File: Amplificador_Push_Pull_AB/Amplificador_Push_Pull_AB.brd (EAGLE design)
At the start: 99 x 49.8 mm, 51 parts, among them IC1 LM741P, IC3 788TV, P2 10k, Q1 BC547, Q10 TIP42C, Q2 BC547, Q4 BC547, Q7 BC547, Q8 BC547, T2 2SC1307

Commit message: Error found and corrected.
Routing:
- net P1: track 61.7 -> 60.9 mm
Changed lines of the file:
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@@
 <wire x1="50.8" y1="25.4" x2="53.975" y2="28.575" width="0.8128" layer="16"/>
 <wire x1="49.53" y1="24.13" x2="50.8" y2="25.4" width="0.8128" layer="16"/>
-<wire x1="43.18" y1="18.415" x2="49.53" y2="18.415" width="0.8128" layer="16"/>
 <wire x1="20.32" y1="8.255" x2="17.145" y2="11.43" width="0.8128" layer="16"/>
 <wire x1="17.145" y1="11.43" x2="17.145" y2="12.065" width="0.8128" layer="16"/>
-<wire x1="43.18" y1="18.415" x2="42.545" y2="17.78" width="0.8128" layer="16"/>
-<wire x1="42.545" y1="17.78" x2="42.545" y2="16.51" width="0.8128" layer="16"/>
-<wire x1="42.545" y1="16.51" x2="39.37" y2="13.335" width="0.8128" layer="16"/>
+<wire x1="44.45" y1="18.415" x2="39.37" y2="13.335" width="0.8128" layer="16"/>
 <wire x1="39.37" y1="13.335" x2="39.37" y2="12.065" width="0.8128" layer="16"/>
 <wire x1="39.37" y1="12.065" x2="37.465" y2="10.16" width="0.8128" layer="16"/>
 <wire x1="37.465" y1="10.16" x2="37.465" y2="8.255" width="0.8128" layer="16"/>
+<wire x1="44.45" y1="18.415" x2="49.53" y2="18.415" width="0.8128" layer="16"/>
 </signal>
 <signal name="N$15">
@@
 <wire x1="29.21" y1="11.43" x2="27.94" y2="10.16" width="0.8128" layer="16"/>
 <wire x1="27.94" y1="10.16" x2="27.94" y2="7.62" width="0.8128" layer="16"/>
-<wire x1="21.59" y1="2.54" x2="36.83" y2="2.54" width="1.27" layer="16"/>
-<wire x1="36.83" y1="2.54" x2="37.465" y2="3.175" width="0.8128" layer="16"/>
-<wire x1="37.465" y1="3.175" x2="42.545" y2="3.175" width="0.8128" layer="16"/>
+<wire x1="21.59" y1="2.54" x2="41.91" y2="2.54" width="1.27" layer="16"/>
 <wire x1="54.61" y1="17.78" x2="51.435" y2="14.605" width="1.27" layer="16"/>
 <wire x1="51.435" y1="14.605" x2="49.53" y2="14.605" width="1.27" layer="16"/>
@@
 <wire x1="43.18" y1="8.255" x2="42.545" y2="8.255" width="1.27" layer="16"/>
 <wire x1="57.785" y1="14.605" x2="57.785" y2="17.78" width="0.8128" layer="16"/>
+<wire x1="41.91" y1="2.54" x2="42.545" y2="3.175" width="1.27" layer="16"/>
 </signal>
 <signal name="N$23">

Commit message: Separate fround line done. Its resistance is approximately 0.1 ohm. Schematic connections integrity verified. Check DRC next time!
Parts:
- moved C1 2.54 mm to (81.3, 41.9)
- moved VCC 1.27 mm to (5.71, 33.0)
- moved RCA1 0.64 mm to (17.8, 45.1)
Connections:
- net N$24 renamed +5V
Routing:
- net GND: track 270.7 -> 364.1 mm
- net N$5: track 27.2 -> 30.6 mm
- net VOUT: track 57.4 -> 59.5 mm
- net -18V: track 177.1 -> 175.8 mm
- net +18V: track 162.7 -> 163.4 mm
- net HEHEAH: track 66.6 -> 65.8 mm
- removed copper zone on layer 16, net GND

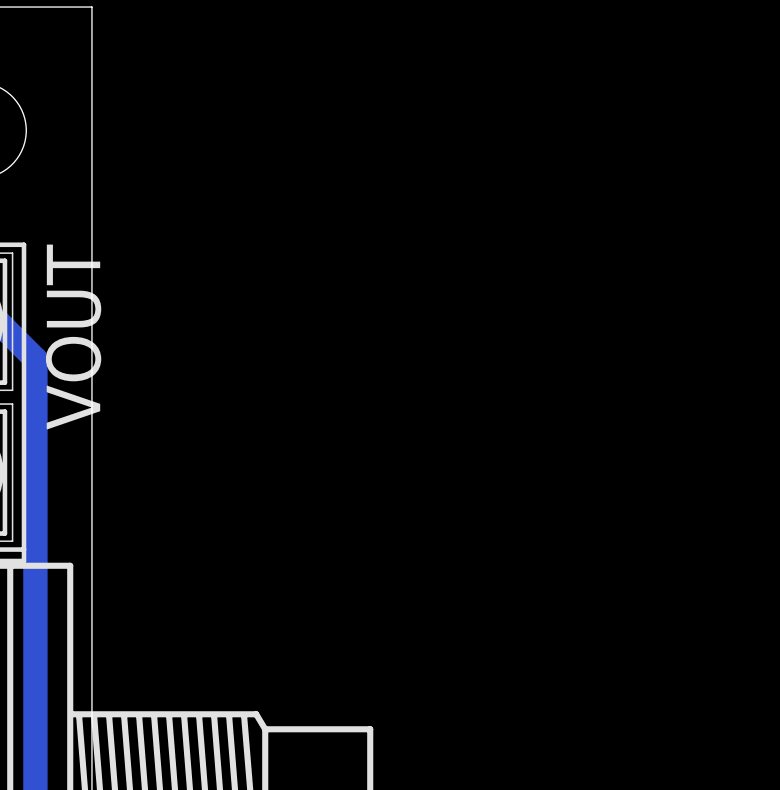
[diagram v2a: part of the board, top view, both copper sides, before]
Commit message: Led added on schematic. Need to put allocate it in board now.
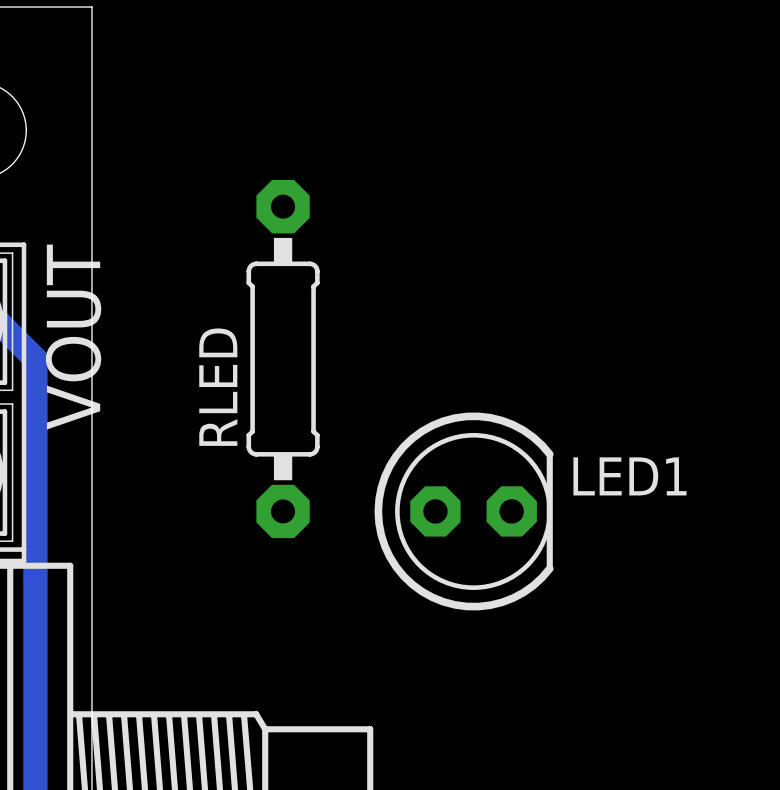
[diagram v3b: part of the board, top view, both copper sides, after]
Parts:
- added LED1: (no value), adafruit:LED5MM
- added RLED: 330, rcl:0207/10
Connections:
- new net N$18: LED1.K, RLED.1
- net +5V: now also LED1.A
- net GND: now also RLED.2
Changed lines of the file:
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@@
 <wire x1="99.04" y1="49.835" x2="0" y2="49.835" width="0" layer="20"/>
 <wire x1="0" y1="49.835" x2="0" y2="0" width="0" layer="20"/>
-<dimension x1="0" y1="0" x2="0" y2="49.53" x3="-3.81" y3="24.765" textsize="1.778" layer="1"/>
-<dimension x1="0" y1="0" x2="99.06" y2="0" x3="49.53" y3="-10.16" textsize="1.778" layer="1"/>
 <hole x="3.81" y="3.81" drill="3.2"/>
 <hole x="3.81" y="45.72" drill="3.2"/>
@@
 <element name="RLEFT" library="rcl" package="0207/7" value="10k" x="77.47" y="6.985" rot="R90"/>
 <element name="IC3" library="linear" package="TO220V" value="788TV" x="80.01" y="38.1"/>
+<element name="LED1" library="adafruit" package="LED5MM" value="" x="111.76" y="33.02"/>
+<element name="RLED" library="rcl" package="0207/10" value="330" x="105.41" y="38.1" rot="R90"/>
 </elements>
 <signals>
@@
 <wire x1="8.255" y1="17.78" x2="10.16" y2="15.875" width="0.8128" layer="16"/>
 <wire x1="10.16" y1="15.875" x2="10.795" y2="15.875" width="0.8128" layer="16"/>
-<wire x1="8.255" y1="26.67" x2="8.255" y2="22.86" width="0" layer="19" extent="16-16"/>
 <via x="10.795" y="15.875" extent="1-16" drill="0.8" diameter="1.6764" shape="octagon"/>
+<contactref element="RLED" pad="2"/>
+<wire x1="97.155" y1="38.1" x2="105.41" y2="43.18" width="0" layer="19" extent="16-16"/>
+<wire x1="8.255" y1="22.86" x2="8.255" y2="26.67" width="0" layer="19" extent="16-16"/>
 </signal>
 <signal name="N$13">
@@
 <wire x1="84.455" y1="28.575" x2="86.995" y2="26.035" width="0.8128" layer="16"/>
 <wire x1="86.995" y1="26.035" x2="90.805" y2="26.035" width="0.8128" layer="16"/>
+<contactref element="LED1" pad="A"/>
+<wire x1="90.805" y1="26.035" x2="110.49" y2="33.02" width="0" layer="19" extent="1-1"/>
 </signal>
 <signal name="N$22">
@@
 <wire x1="13.335" y1="42.545" x2="13.335" y2="39.37" width="0.8128" layer="16"/>
 </signal>
+<signal name="N$18">
+<contactref element="LED1" pad="K"/>
+<contactref element="RLED" pad="1"/>
+<wire x1="105.41" y1="33.02" x2="113.03" y2="33.02" width="0" layer="19" extent="1-1"/>
+</signal>
 </signals>
